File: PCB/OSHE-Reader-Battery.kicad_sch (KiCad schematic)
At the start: 17 parts, among them Q1 PNP, Q2 PMOS, U2 BQ2057CSNTR

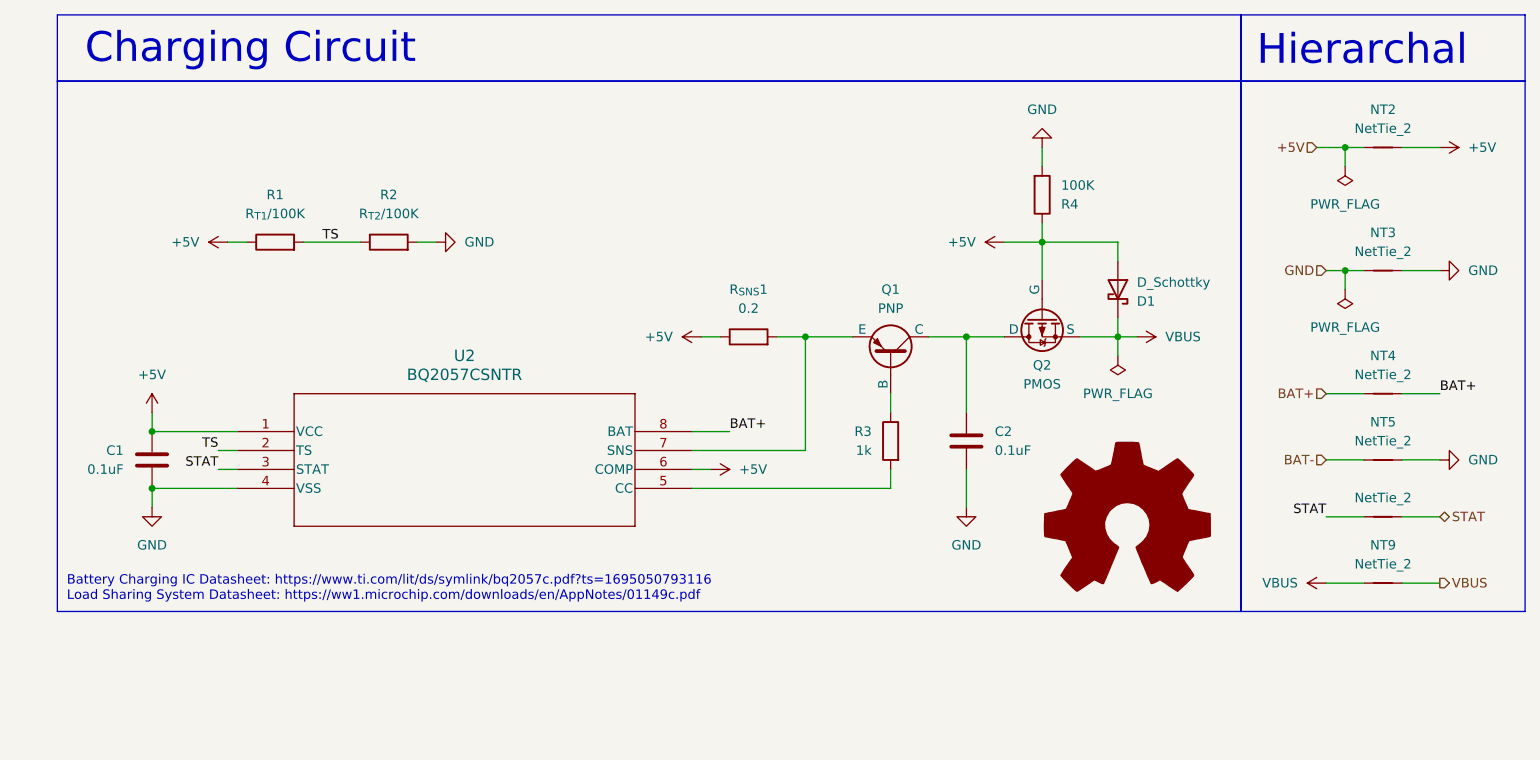
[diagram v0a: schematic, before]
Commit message: updated battery charging and overall sheet with new mosfet + diode symbol
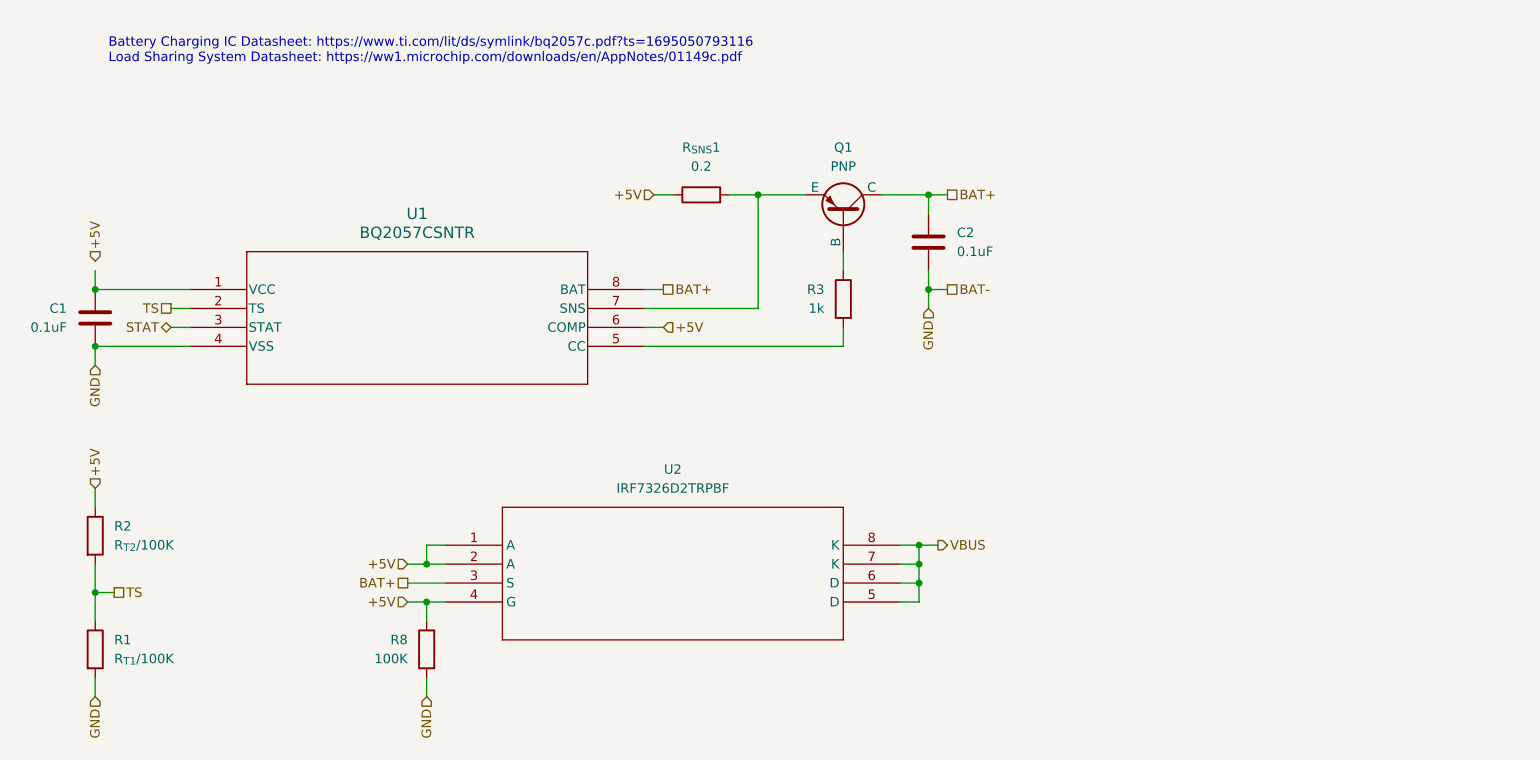
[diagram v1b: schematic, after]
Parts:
- removed D1: D_Schottky, symbol Device:D_Schottky
- removed NT2, NT3, NT4, NT5, NT7, NT9: NetTie_2, symbol Device:NetTie_2
- removed Q2: PMOS, symbol Simulation_SPICE:PMOS
- removed R4: 100K, symbol Device:R
- added R8: 100K, symbol Device:R
- added U2: IRF7326D2TRPBF, Package_SO:SO-8_3.9x4.9mm_P1.27mm, symbol IRF7326D2TRPBF:IRF7326D2TRPBF
- renumbered U2 to U1
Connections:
- net +5V: now also R2.1, R8.1, U2.1 (A), U2.2 (A), U2.4 (G); no longer C1.1, R1.1, U1.1 (VCC)
- net BAT+: now also C2.1, Q1.1 (C), U2.3 (S)
- net BAT-: now also C1.2, C2.2, R1.2, U1.4 (VSS), R8.2
- net TS: now also R1.1, R2.2; no longer R1.2, R2.1
- net VBUS: now also U2.5 (D), U2.6 (D), U2.7 (K), U2.8 (K)
- removed net GND: C1.2, C2.2, R2.2, U1.4 (VSS)
- new net: C1.1, U1.1 (VCC)
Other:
- note removed: "Charging Circuit"
- note removed: "Hierarchal"
- moved on the sheet: C1, C2, Q1, R1, R2, R3, R_{SNS}1, U1

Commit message: added hierarchical symbols to Buck, and did miscelaneous fixes
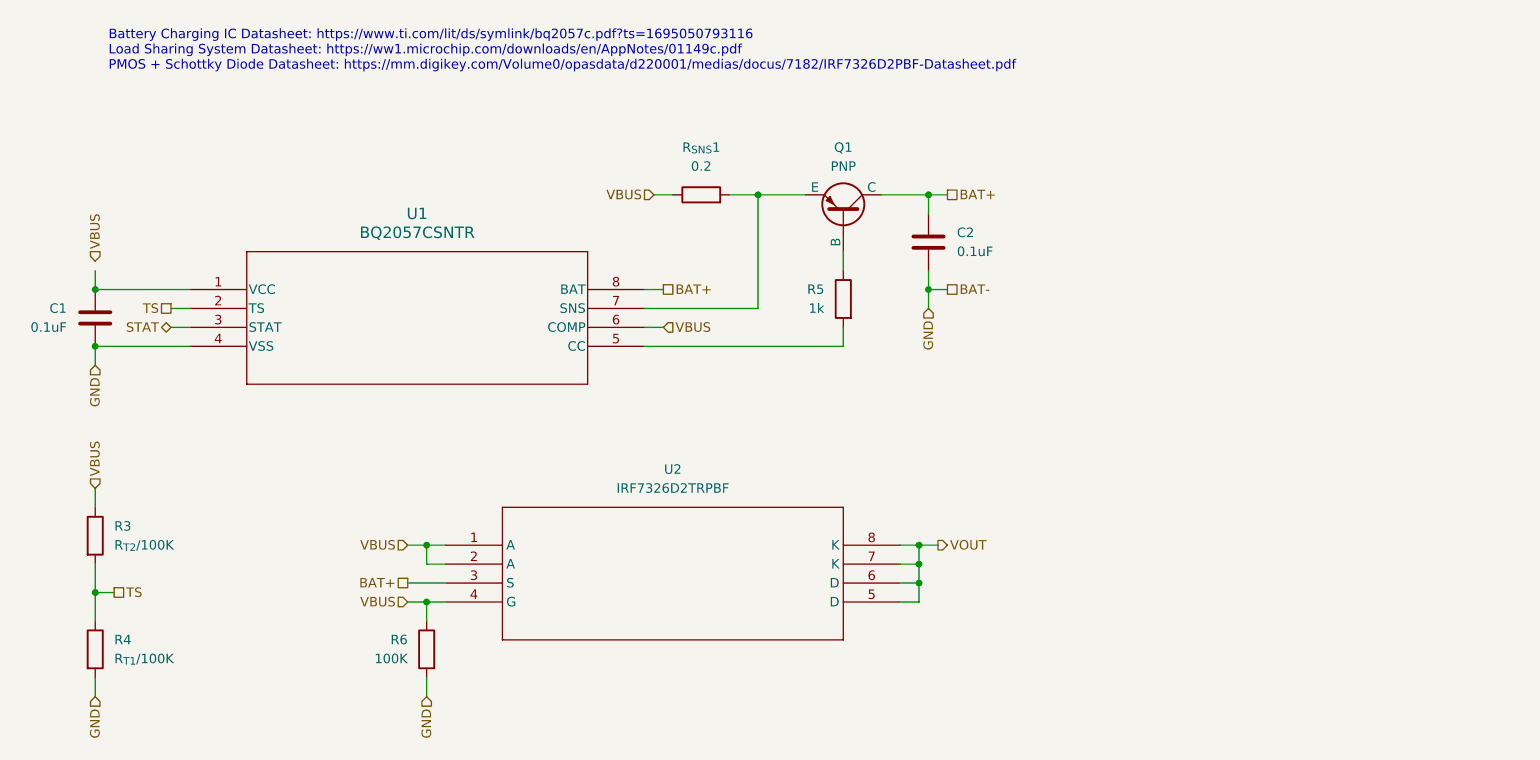
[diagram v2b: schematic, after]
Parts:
- renumbered R2 to R3, R1 to R4, R3 to R5, R8 to R6
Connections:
- net +5V is gone; now on net VBUS: R3.1, R6.1, R_{SNS}1.1, U1.6 (COMP), U2.1 (A), U2.2 (A), U2.4 (G)
- net VBUS: no longer U2.5 (D), U2.6 (D), U2.7 (K), U2.8 (K)
- new net VOUT: U2.5 (D), U2.6 (D), U2.7 (K), U2.8 (K)
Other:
- note added: "Battery Charging IC Datasheet: https://www.ti.com/lit/ds/symlink/bq2057c.pdf?ts=1695050793116 Load Sharing System Datasheet: https://ww1.microchip.com/downloads/en/AppNotes/01149c.pdf PMOS + Schottky Diode Datasheet: https://mm.digikey.com/Volume0/opasdata/d220001/medias/docus/7182/IRF7326D2PBF-Datasheet.pdf"
- note removed: "Battery Charging IC Datasheet: https://www.ti.com/lit/ds/symlink/bq2057c.pdf?ts=1695050793116 Load Sharing System Datasheet: https://ww1.microchip.com/downloads/en/AppNotes/01149c.pdf"

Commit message: fixed up the pcb so everything is *basically* passing ERC
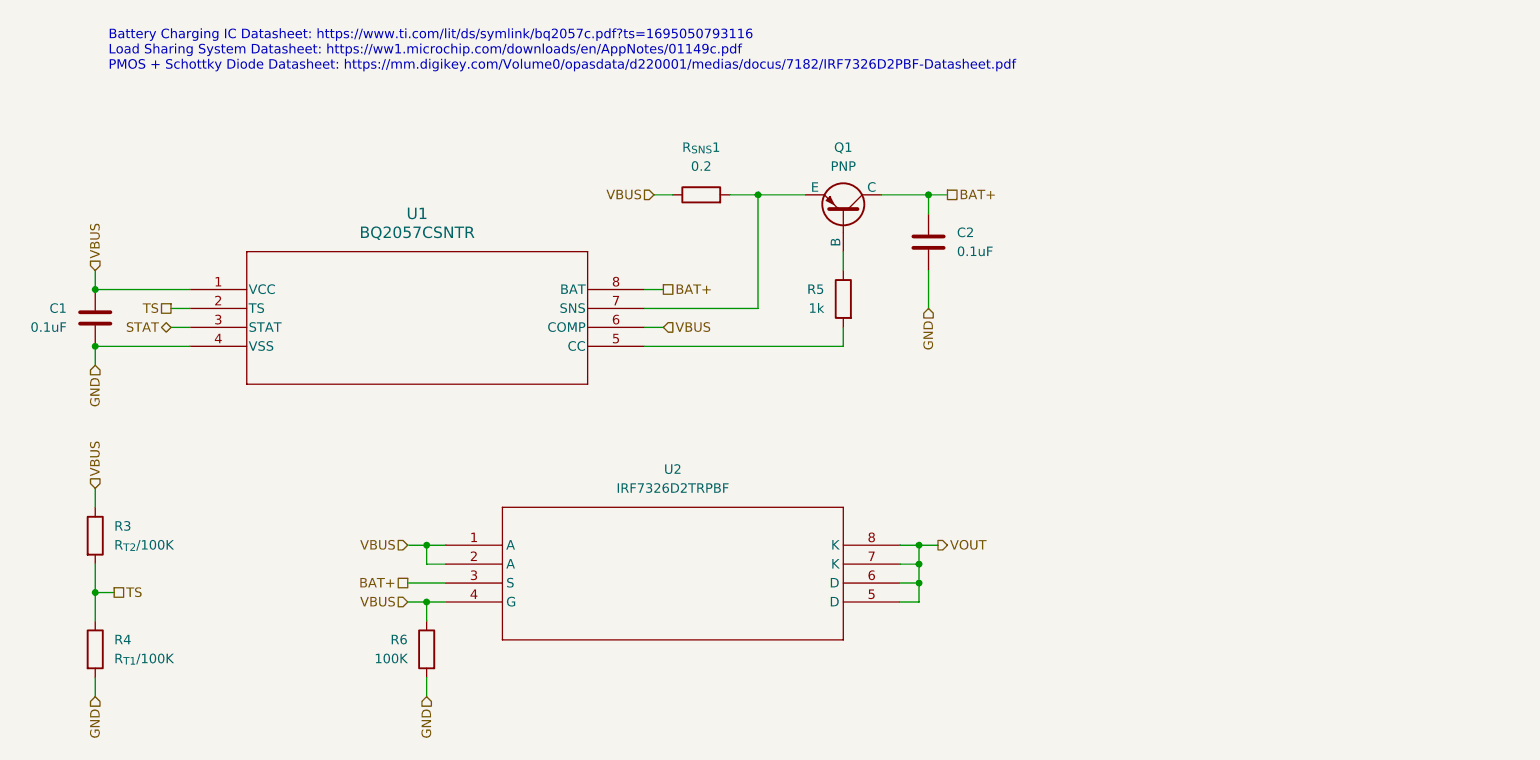
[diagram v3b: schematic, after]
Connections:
- net VBUS: now also C1.1, U1.1 (VCC)
- net BAT- renamed GND

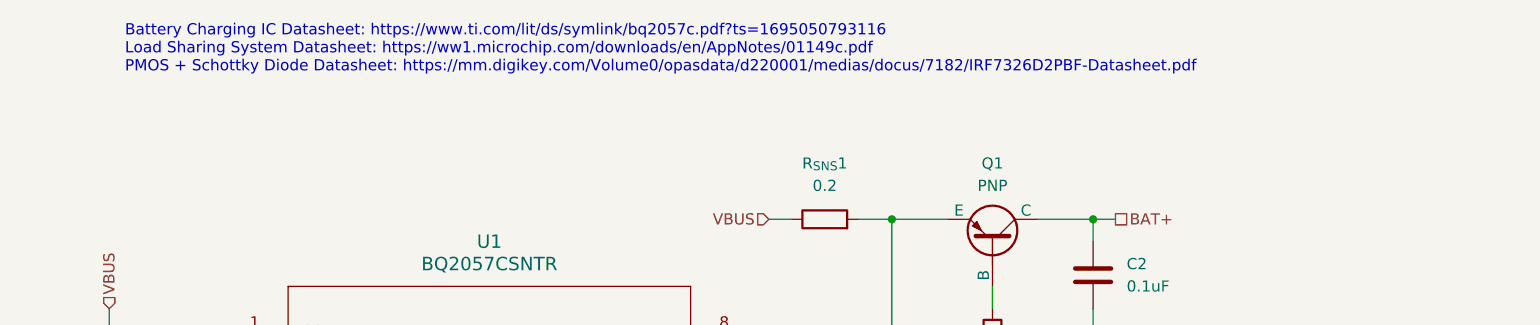
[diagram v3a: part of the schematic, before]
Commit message: work on pcb, adjusted components and started building ribbon connector for display
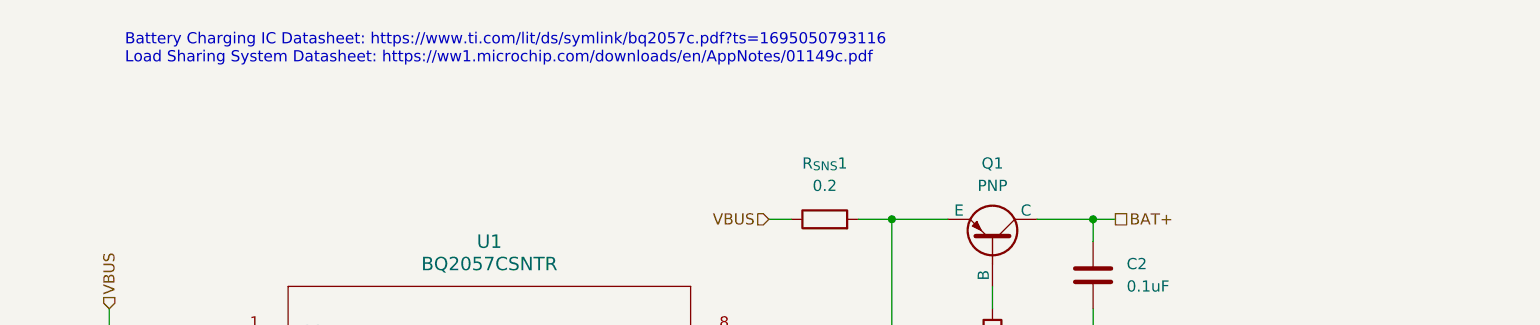
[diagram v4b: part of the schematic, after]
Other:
- note added: "Battery Charging IC Datasheet: https://www.ti.com/lit/ds/symlink/bq2057c.pdf?ts=1695050793116 Load Sharing System Datasheet: https://ww1.microchip.com/downloads/en/AppNotes/01149c.pdf"
- note removed: "Battery Charging IC Datasheet: https://www.ti.com/lit/ds/symlink/bq2057c.pdf?ts=1695050793116 Load Sharing System Datasheet: https://ww1.microchip.com/downloads/en/AppNotes/01149c.pdf PMOS + Schottky Diode Datasheet: https://mm.digikey.com/Volume0/opasdata/d220001/medias/docus/7182/IRF7326D2PBF-Datasheet.pdf"
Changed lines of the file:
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@@
 	(generator_version "9.0")
 	(paper "A4")
-	(text "Battery Charging IC Datasheet: https://www.ti.com/lit/ds/symlink/bq2057c.pdf?ts=1695050793116\nLoad Sharing System Datasheet: https://ww1.microchip.com/downloads/en/AppNotes/01149c.pdf\nPMOS + Schottky Diode Datasheet: https://mm.digikey.com/Volume0/opasdata/d220001/medias/docus/7182/IRF7326D2PBF-Datasheet.pdf"
+	(text "Battery Charging IC Datasheet: https://www.ti.com/lit/ds/symlink/bq2057c.pdf?ts=1695050793116\nLoad Sharing System Datasheet: https://ww1.microchip.com/downloads/en/AppNotes/01149c.pdf"
 		(exclude_from_sim no)
 		(at 28.448 26.416 0)

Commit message: misc work on schematic
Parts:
- added R_{SNS}2: 0.1, WSL2512R1000FEA:RES_2512_WSL, symbol Device:R
- R_{SNS}1: value 0.2 -> 0.1; footprint (none) -> WSL2512R1000FEA:RES_2512_WSL
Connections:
- net at Q1.3 (E), U1.7 (SNS): now also R_{SNS}2.2; no longer R_{SNS}1.2
- new net: R_{SNS}1.2, R_{SNS}2.1
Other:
- moved on the sheet: R_{SNS}1
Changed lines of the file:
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@@
 	(wire
 		(pts
-			(xy 115.57 45.72) (xy 111.76 45.72)
+			(xy 115.57 45.72) (xy 113.03 45.72)
 		)
 		(stroke
@@
 	(wire
 		(pts
+			(xy 105.41 45.72) (xy 102.87 45.72)
+		)
+		(stroke
+			(width 0)
+			(type default)
+		)
+	)
+	(wire
+		(pts
 			(xy 137.16 100.33) (xy 134.62 100.33)
 		)
@@
 	(wire
 		(pts
-			(xy 101.6 45.72) (xy 104.14 45.72)
+			(xy 92.71 45.72) (xy 95.25 45.72)
 		)
 		(stroke
@@
 	(hierarchical_label "VBUS"
 		(shape input)
-		(at 101.6 45.72 180)
+		(at 92.71 45.72 180)
 		(effects
 			(font
@@
 	(symbol
 		(lib_id "Device:R")
-		(at 107.95 45.72 90)
+		(at 99.06 45.72 90)
 		(unit 1)
 		(exclude_from_sim no)
@@
 		(fields_autoplaced yes)
 		(property "Reference" "R_{SNS}1"
-			(at 107.95 39.37 90)
-			(effects
-				(font
-					(size 1.27 1.27)
-				)
-			)
-		)
-		(property "Value" "0.2"
-			(at 107.95 41.91 90)
-			(effects
-				(font
-					(size 1.27 1.27)
-				)
-			)
-		)
-		(property "Footprint" ""
-			(at 107.95 47.498 90)
+			(at 99.06 39.37 90)
+			(effects
+				(font
+					(size 1.27 1.27)
+				)
+			)
+		)
+		(property "Value" "0.1"
+			(at 99.06 41.91 90)
+			(effects
+				(font
+					(size 1.27 1.27)
+				)
+			)
+		)
+		(property "Footprint" "WSL2512R1000FEA:RES_2512_WSL"
+			(at 99.06 47.498 90)
 			(effects
 				(font
@@
 		)
 		(property "Datasheet" "~"
-			(at 107.95 45.72 0)
+			(at 99.06 45.72 0)
 			(effects
 				(font
@@
 		)
 		(property "Description" "Resistor"
-			(at 107.95 45.72 0)
+			(at 99.06 45.72 0)
 			(effects
 				(font
@@
 					(unit 1)
 				)
+			)
+		)
+	)
+	(symbol
+		(lib_id "Device:R")
+		(at 109.22 45.72 90)
+		(unit 1)
+		(exclude_from_sim no)
+		(in_bom yes)
+		(on_board yes)
+		(dnp no)
+		(fields_autoplaced yes)
+		(property "Reference" "R_{SNS}2"
+			(at 109.22 39.37 90)
+			(effects
+				(font
+					(size 1.27 1.27)
+				)
+			)
+		)
+		(property "Value" "0.1"
+			(at 109.22 41.91 90)
+			(effects
+				(font
+					(size 1.27 1.27)
+				)
+			)
+		)
+		(property "Footprint" "WSL2512R1000FEA:RES_2512_WSL"
+			(at 109.22 47.498 90)
+			(effects
+				(font
+					(size 1.27 1.27)
+				)
+				(hide yes)
+			)
+		)
+		(property "Datasheet" "~"
+			(at 109.22 45.72 0)
+			(effects
+				(font
+					(size 1.27 1.27)
+				)
+				(hide yes)
+			)
+		)
+		(property "Description" "Resistor"
+			(at 109.22 45.72 0)
+			(effects
+				(font
+					(size 1.27 1.27)
+				)
+				(hide yes)
+			)
+		)
+		(pin "2"
+		)
+		(pin "1"
+		)
+		(instances
+			(project "OSHE-Reader-PCB"
+				(path "/3f072c92-e35a-4654-839b-728bd3dc3a46/9b683008-b3f5-4049-bcf9-7e8cdd298ddd"
+					(reference "R_{SNS}2")
+					(unit 1)
+				)

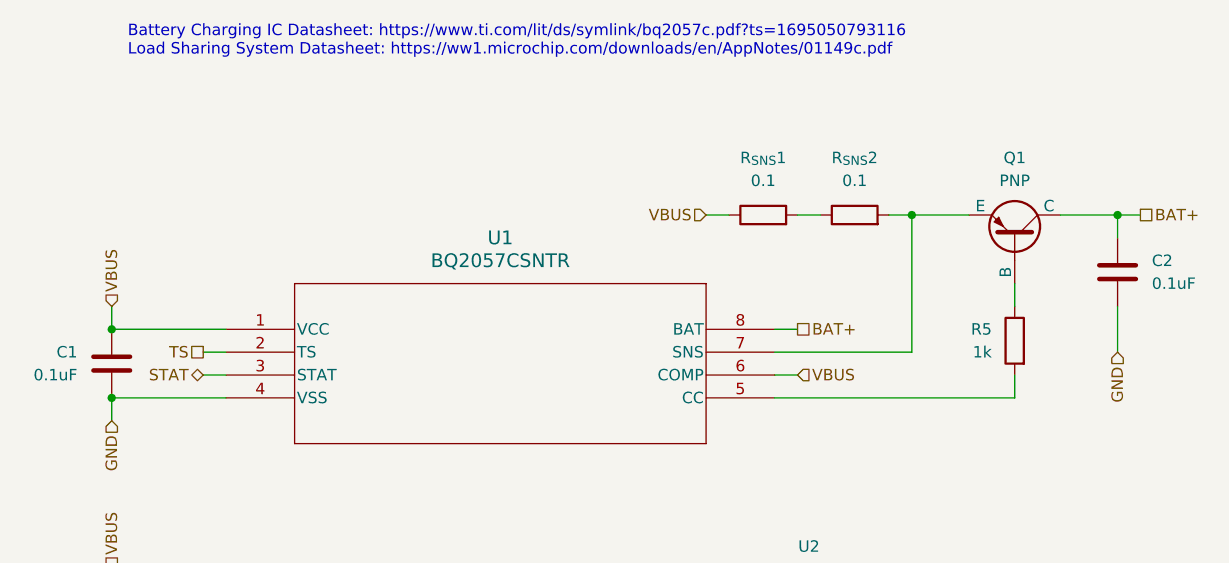
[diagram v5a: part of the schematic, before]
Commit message: fixed mislabeling of pins on battery charging IC
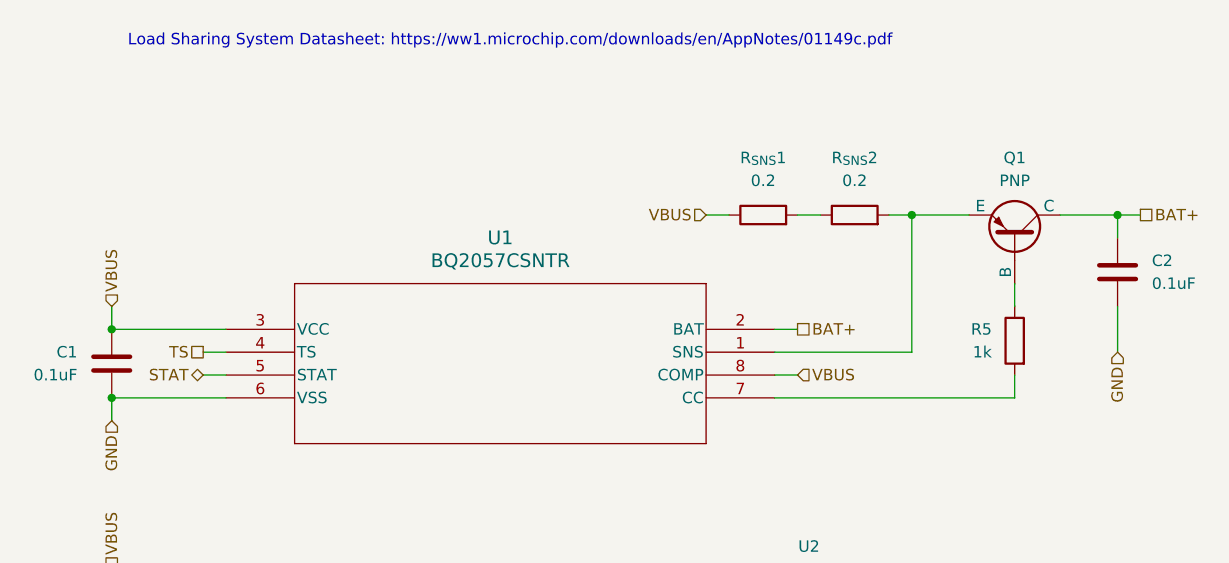
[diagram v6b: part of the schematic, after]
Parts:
- R_{SNS}1, R_{SNS}2: value 0.1 -> 0.2
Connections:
- net BAT+: now also U1.2 (BAT); no longer U1.8 (BAT)
- net GND: now also U1.6 (VSS); no longer U1.4 (VSS)
- net STAT: now also U1.5 (STAT); no longer U1.3 (STAT)
- net TS: now also U1.4 (TS); no longer U1.2 (TS)
- net VBUS: now also U1.3 (VCC), U1.8 (COMP); no longer U1.1 (VCC), U1.6 (COMP)
- net at R5.2: now also U1.7 (CC); no longer U1.5 (CC)
- net at Q1.3 (E), R_{SNS}2.2: now also U1.1 (SNS); no longer U1.7 (SNS)
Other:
- note added: "Load Sharing System Datasheet: https://ww1.microchip.com/downloads/en/AppNotes/01149c.pdf"
- note removed: "Battery Charging IC Datasheet: https://www.ti.com/lit/ds/symlink/bq2057c.pdf?ts=1695050793116 Load Sharing System Datasheet: https://ww1.microchip.com/downloads/en/AppNotes/01149c.pdf"
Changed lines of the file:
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@@
 	(generator_version "9.0")
 	(paper "A4")
-	(text "Battery Charging IC Datasheet: https://www.ti.com/lit/ds/symlink/bq2057c.pdf?ts=1695050793116\nLoad Sharing System Datasheet: https://ww1.microchip.com/downloads/en/AppNotes/01149c.pdf"
+	(text "Load Sharing System Datasheet: https://ww1.microchip.com/downloads/en/AppNotes/01149c.pdf"
 		(exclude_from_sim no)
 		(at 28.448 26.416 0)
@@
 			)
 		)
-		(property "Value" "0.1"
+		(property "Value" "0.2"
 			(at 99.06 41.91 90)
 			(effects
@@
 			)
 		)
-		(property "Value" "0.1"
+		(property "Value" "0.2"
 			(at 109.22 41.91 90)
 			(effects
